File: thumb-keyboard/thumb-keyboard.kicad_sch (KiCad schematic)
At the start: 132 parts, among them J1 Conn_01x02_Socket, U1 nice_nano

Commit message: first commit after change to branch with optional B3F-1000 switches. footprint is going to be 144x60
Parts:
- added S100, S101, S102, S103, S104, S105, S106, S107, S108, S109, S110, S111, S112, S113, S114, S115, S116, S117, S118, S119, S120, S123, S61, S62, S64, S65, S66, S67, S68, S69, S70, S71, S72, S73, S74, S75, S76, S77, S78, S79, S80, S81, S82, S83, S84, S85, S86, S87, S88, S89, S90, S91, S92, S93, S94, S95, S96, S97, S98, S99: B3F-1000, B3F_1000:SW_B3F-1000, symbol B3F-1000:B3F-1000
- renumbered S62 to S121, S61 to S122
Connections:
- net C0R0D: now also S61.3, S61.4; no longer S63.1, S63.2
- net COL0: now also S109.1, S109.2, S61.1, S61.2, S73.1, S73.2, S85.1, S85.2, S97.1, S97.2; no longer S63.3, S63.4
- net COL1: now also S110.1, S110.2, S62.1, S62.2, S74.1, S74.2, S86.1, S86.2, S98.1, S98.2; no longer U1.12 (P1.06)
- net COL10: now also U1.20 (AIN7/P0.31), S107.1, S107.2, S119.1, S119.2, S71.1, S71.2, S83.1, S83.2, S95.1, S95.2
- net COL11: now also S108.1, S108.2, S120.1, S120.2, S72.1, S72.2, S84.1, S84.2, S96.1, S96.2
- net COL2: now also S63.1, S63.2, S111.1, S111.2, S75.1, S75.2, S87.1, S87.2, S99.1, S99.2
- net COL3: now also S100.1, S100.2, S112.1, S112.2, S64.1, S64.2, S76.1, S76.2, S88.1, S88.2
- net COL4: now also S101.1, S101.2, S113.1, S113.2, S65.1, S65.2, S77.1, S77.2, S89.1, S89.2
- net COL5: now also S102.1, S102.2, S114.1, S114.2, S66.1, S66.2, S78.1, S78.2, S90.1, S90.2
- net COL6: now also S103.1, S103.2, S115.1, S115.2, S67.1, S67.2, S79.1, S79.2, S91.1, S91.2
- net COL7: now also S104.1, S104.2, S116.1, S116.2, S68.1, S68.2, S80.1, S80.2, S92.1, S92.2
- net COL8: now also S105.1, S105.2, S117.1, S117.2, S69.1, S69.2, S81.1, S81.2, S93.1, S93.2
- net COL9: now also U1.12 (P1.06), S106.1, S106.2, S118.1, S118.2, S70.1, S70.2, S82.1, S82.2, S94.1, S94.2
- net GND: now also S123.3, S123.4
- net ROW2: no longer U1.20 (AIN7/P0.31)
- net RST: now also S123.1, S123.2
- net C7R2D: now reaches D32.2 (A), S32.3, S32.4
- net C7R2D: now also S92.3, S92.4
- net C5R2D: now reaches D30.2 (A), S30.3, S30.4
- net C5R2D: now also S90.3, S90.4
- net C2R2D: now reaches D27.2 (A), S27.3, S27.4
- net C2R2D: now also S87.3, S87.4
- net C1R0D: now reaches D2.2 (A), S2.3, S2.4
- net C1R0D: now also S62.3, S62.4
- net C4R4D: now reaches D53.2 (A), S53.3, S53.4
- net C4R4D: now also S113.3, S113.4
- net C11R2D: now reaches D36.2 (A), S36.3, S36.4
- net C11R2D: now also S96.3, S96.4
- net C4R0D: now reaches D5.2 (A), S5.3, S5.4
- net C4R0D: now also S65.3, S65.4
- net C3R4D: now reaches D52.2 (A), S52.3, S52.4
- net C3R4D: now also S112.3, S112.4
- net C6R2D: now reaches D31.2 (A), S31.3, S31.4
- net C6R2D: now also S91.3, S91.4
- net C9R2D: now reaches D34.2 (A), S34.3, S34.4
- net C9R2D: now also S94.3, S94.4
- net C8R2D: now reaches D33.2 (A), S33.3, S33.4
- net C8R2D: now also S93.3, S93.4
- net C1R4D: now reaches D50.2 (A), S50.3, S50.4
- net C1R4D: now also S110.3, S110.4
- net C10R2D: now reaches D35.2 (A), S35.3, S35.4
- net C10R2D: now also S95.3, S95.4
- net C6R1D: now reaches D19.2 (A), S19.3, S19.4
- net C6R1D: now also S79.3, S79.4
- net C9R1D: now reaches D22.2 (A), S22.3, S22.4
- net C9R1D: now also S82.3, S82.4
- net C2R1D: now reaches D15.2 (A), S15.3, S15.4
- net C2R1D: now also S75.3, S75.4
- net C0R3D: now reaches D37.2 (A), S37.3, S37.4
- net C0R3D: now also S97.3, S97.4
- net C9R0D: now reaches D10.2 (A), S10.3, S10.4
- net C9R0D: now also S70.3, S70.4
- net C5R4D: now reaches D54.2 (A), S54.3, S54.4
- net C5R4D: now also S114.3, S114.4
- net C0R1D: now reaches D13.2 (A), S13.3, S13.4
- net C0R1D: now also S73.3, S73.4
- net C11R1D: now reaches D24.2 (A), S24.3, S24.4
- net C11R1D: now also S84.3, S84.4
- net C9R4D: now reaches D58.2 (A), S58.3, S58.4
- net C9R4D: now also S118.3, S118.4
- net C4R1D: now reaches D17.2 (A), S17.3, S17.4
- net C4R1D: now also S77.3, S77.4
- net C11R0D: now reaches D12.2 (A), S12.3, S12.4
- net C11R0D: now also S72.3, S72.4
- net C2R3D: now reaches D39.2 (A), S39.3, S39.4
- net C2R3D: now also S99.3, S99.4
- net C10R4D: now reaches D59.2 (A), S59.3, S59.4
- net C10R4D: now also S119.3, S119.4
- net C1R3D: now reaches D38.2 (A), S38.3, S38.4
- net C1R3D: now also S98.3, S98.4
- net C0R4D: now reaches D49.2 (A), S49.3, S49.4
- net C0R4D: now also S109.3, S109.4
- net C0R2D: now reaches D25.2 (A), S25.3, S25.4
- net C0R2D: now also S85.3, S85.4
- net C5R0D: now reaches D6.2 (A), S6.3, S6.4
- net C5R0D: now also S66.3, S66.4
- net C5R1D: now reaches D18.2 (A), S18.3, S18.4
- net C5R1D: now also S78.3, S78.4
- net C6R0D: now reaches D7.2 (A), S7.3, S7.4
- net C6R0D: now also S67.3, S67.4
- net C11R3D: now reaches D48.2 (A), S48.3, S48.4
- net C11R3D: now also S108.3, S108.4
- net C4R3D: now reaches D41.2 (A), S41.3, S41.4
- net C4R3D: now also S101.3, S101.4
- net C10R0D: now reaches D11.2 (A), S11.3, S11.4
- net C10R0D: now also S71.3, S71.4
- net C11R4D: now reaches D60.2 (A), S60.3, S60.4
- net C11R4D: now also S120.3, S120.4
- net C10R3D: now reaches D47.2 (A), S47.3, S47.4
- net C10R3D: now also S107.3, S107.4
- net C2R4D: now reaches D51.2 (A), S51.3, S51.4
- net C2R4D: now also S111.3, S111.4
- net C1R2D: now reaches D26.2 (A), S26.3, S26.4
- net C1R2D: now also S86.3, S86.4
- net C7R1D: now reaches D20.2 (A), S20.3, S20.4
- net C7R1D: now also S80.3, S80.4
- net C3R1D: now reaches D16.2 (A), S16.3, S16.4
- net C3R1D: now also S76.3, S76.4
- net C6R4D: now reaches D55.2 (A), S55.3, S55.4
- net C6R4D: now also S115.3, S115.4
- net C3R3D: now reaches D40.2 (A), S40.3, S40.4
- net C3R3D: now also S100.3, S100.4
- net C8R0D: now reaches D9.2 (A), S9.3, S9.4
- net C8R0D: now also S69.3, S69.4
- net C10R1D: now reaches D23.2 (A), S23.3, S23.4
- net C10R1D: now also S83.3, S83.4
- net C4R2D: now reaches D29.2 (A), S29.3, S29.4
- net C4R2D: now also S89.3, S89.4
- net C2R0D: now reaches D3.2 (A), S3.3, S3.4
- net C2R0D: now also S63.3, S63.4
- net C7R0D: now reaches D8.2 (A), S8.3, S8.4
- net C7R0D: now also S68.3, S68.4
- net C8R4D: now reaches D57.2 (A), S57.3, S57.4
- net C8R4D: now also S117.3, S117.4
- net C8R1D: now reaches D21.2 (A), S21.3, S21.4
- net C8R1D: now also S81.3, S81.4
- net C7R3D: now reaches D44.2 (A), S44.3, S44.4
- net C7R3D: now also S104.3, S104.4
- net C6R3D: now reaches D43.2 (A), S43.3, S43.4
- net C6R3D: now also S103.3, S103.4
- net C9R3D: now reaches D46.2 (A), S46.3, S46.4
- net C9R3D: now also S106.3, S106.4
- net C5R3D: now reaches D42.2 (A), S42.3, S42.4
- net C5R3D: now also S102.3, S102.4
- net C3R2D: now reaches D28.2 (A), S28.3, S28.4
- net C3R2D: now also S88.3, S88.4
- net C7R4D: now reaches D56.2 (A), S56.3, S56.4
- net C7R4D: now also S116.3, S116.4
- net C8R3D: now reaches D45.2 (A), S45.3, S45.4
- net C8R3D: now also S105.3, S105.4
- net C1R1D: now reaches D14.2 (A), S14.3, S14.4
- net C1R1D: now also S74.3, S74.4
- net C3R0D: now reaches D4.2 (A), S4.3, S4.4
- net C3R0D: now also S64.3, S64.4
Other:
- moved on the sheet: D61, D62, D63, D64, D65, D66, D67, S121, S122

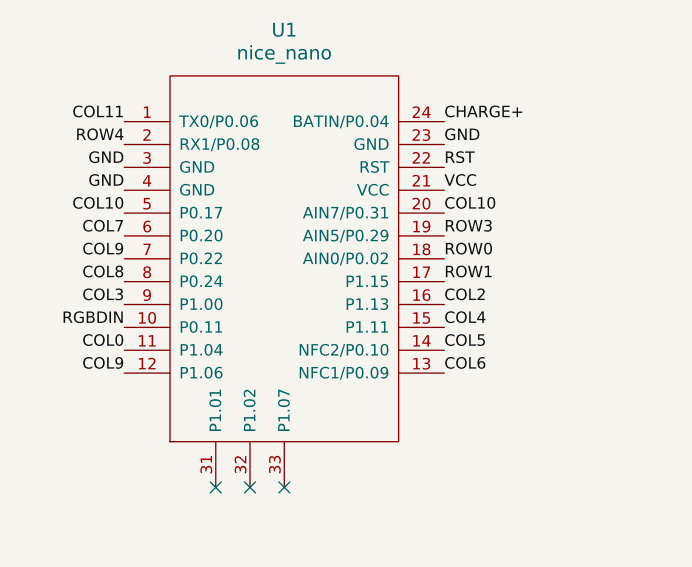
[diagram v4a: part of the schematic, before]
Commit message: have something that looks alright. max size of 144x60mm. A little concerning how messy it is though
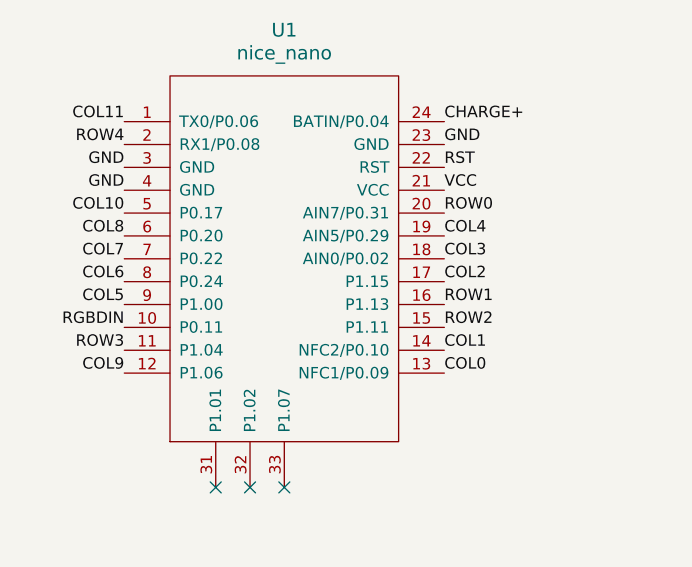
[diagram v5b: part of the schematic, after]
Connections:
- net COL0: now also U1.13 (NFC1/P0.09); no longer U1.11 (P1.04)
- net COL1: now also U1.14 (NFC2/P0.10)
- net COL10: no longer U1.20 (AIN7/P0.31)
- net COL2: now also U1.17 (P1.15); no longer U1.16 (P1.13)
- net COL3: now also U1.18 (AIN0/P0.02); no longer U1.9 (P1.00)
- net COL4: now also U1.19 (AIN5/P0.29); no longer U1.15 (P1.11)
- net COL5: now also U1.9 (P1.00); no longer U1.14 (NFC2/P0.10)
- net COL6: now also U1.8 (P0.24); no longer U1.13 (NFC1/P0.09)
- net COL7: now also U1.7 (P0.22); no longer U1.6 (P0.20)
- net COL8: now also U1.6 (P0.20); no longer U1.8 (P0.24)
- net COL9: no longer U1.7 (P0.22)
- net ROW0: now also U1.20 (AIN7/P0.31); no longer U1.18 (AIN0/P0.02)
- net ROW1: now also U1.16 (P1.13); no longer U1.17 (P1.15)
- net ROW2: now also U1.15 (P1.11)
- net ROW3: now also U1.11 (P1.04); no longer U1.19 (AIN5/P0.29)
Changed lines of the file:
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@@
 		)
 	)
+	(label "COL8"
+		(at 26.67 52.07 180)
+		(effects
+			(font
+				(size 1.27 1.27)
+			)
+			(justify right bottom)
+		)
+	)
 	(label "RST"
 		(at 116.84 488.95 0)
@@
 		)
 	)
-	(label "COL0"
-		(at 26.67 64.77 180)
-		(effects
-			(font
-				(size 1.27 1.27)
-			)
-			(justify right bottom)
-		)
-	)
 	(label "C8R4D"
 		(at 280.67 361.95 0)
@@
 		)
 	)
-	(label "ROW3"
-		(at 62.23 52.07 0)
-		(effects
-			(font
-				(size 1.27 1.27)
-			)
-			(justify left bottom)
-		)
-	)
 	(label "C7R4D"
 		(at 251.46 387.35 0)
@@
 		)
 	)
-	(label "COL5"
-		(at 62.23 64.77 0)
-		(effects
-			(font
-				(size 1.27 1.27)
-			)
-			(justify left bottom)
-		)
-	)
 	(label "COL11"
 		(at 358.14 300.99 180)
@@
 		)
 	)
-	(label "C1R0D"
-		(at 76.2 266.7 0)
+	(label "COL5"
+		(at 26.67 59.69 180)
+		(effects
+			(font
+				(size 1.27 1.27)
+			)
+			(justify right bottom)
+		)
+	)
+	(label "ROW2"
+		(at 62.23 62.23 0)
 		(effects
 			(font
@@
 		)
 	)
-	(label "C7R1D"
-		(at 461.01 71.12 90)
+	(label "C1R0D"
+		(at 76.2 266.7 0)
 		(effects
 			(font
@@
 		)
 	)
-	(label "ROW1"
-		(at 62.23 57.15 0)
+	(label "C7R1D"
+		(at 461.01 71.12 90)
 		(effects
 			(font
@@
 		)
 	)
-	(label "COL3"
-		(at 26.67 59.69 180)
-		(effects
-			(font
-				(size 1.27 1.27)
-			)
-			(justify right bottom)
-		)
-	)
 	(label "C4R0D"
 		(at 163.83 266.7 0)
@@
 		)
 	)
-	(label "COL6"
-		(at 62.23 67.31 0)
-		(effects
-			(font
-				(size 1.27 1.27)
-			)
-			(justify left bottom)
-		)
-	)
 	(label "C6R2D"
 		(at 416.56 96.52 90)
@@
 		)
 	)
-	(label "COL9"
-		(at 26.67 54.61 180)
-		(fields_autoplaced yes)
-		(effects
-			(font
-				(size 1.27 1.27)
-			)
-			(justify right bottom)
-		)
-		(property "Netclass" "Default"
-			(at 26.67 55.88 0)
-			(effects
-				(font
-					(size 1.27 1.27)
-					(italic yes)
-				)
-				(justify right)
-				(hide yes)
-			)
-		)
-	)
 	(label "C8R3D"
 		(at 280.67 331.47 0)
@@
 		)
 	)
+	(label "COL3"
+		(at 62.23 54.61 0)
+		(effects
+			(font
+				(size 1.27 1.27)
+			)
+			(justify left bottom)
+		)
+	)
 	(label "C2R0D"
 		(at 105.41 266.7 0)
@@
 		)
 	)
+	(label "COL7"
+		(at 26.67 54.61 180)
+		(effects
+			(font
+				(size 1.27 1.27)
+			)
+			(justify right bottom)
+		)
+	)
 	(label "COL8"
 		(at 270.51 241.3 180)
@@
 		)
 	)
-	(label "COL2"
-		(at 62.23 59.69 0)
+	(label "C9R3D"
+		(at 549.91 121.92 90)
 		(effects
 			(font
@@
 		)
 	)
-	(label "C9R3D"
-		(at 549.91 121.92 90)
+	(label "ROW3"
+		(at 26.67 64.77 180)
 		(effects
 			(font
 				(size 1.27 1.27)
 			)
-			(justify left bottom)
+			(justify right bottom)
 		)
 	)
@@
 		)
 	)
+	(label "ROW1"
+		(at 62.23 59.69 0)
+		(effects
+			(font
+				(size 1.27 1.27)
+			)
+			(justify left bottom)
+		)
+	)
 	(label "C5R2D"
 		(at 372.11 96.52 90)
@@
 		)
 	)
-	(label "ROW4"
-		(at 26.67 41.91 180)
-		(fields_autoplaced yes)
-		(effects
-			(font
-				(size 1.27 1.27)
-			)
-			(justify right bottom)
-		)
-		(property "Netclass" "Default"
-			(at 26.67 43.18 0)
-			(effects
-				(font
-					(size 1.27 1.27)
-					(italic yes)
-				)
-				(justify right)
-				(hide yes)
-			)
-		)
-	)
 	(label "GND"
 		(at 199.39 185.42 0)
@@
 		)
 	)
-	(label "ROW0"
-		(at 62.23 54.61 0)
-		(effects
-			(font
-				(size 1.27 1.27)
-			)
-			(justify left bottom)
-		)
-	)
 	(label "C0R1D"
 		(at 46.99 295.91 0)
@@
 		)
 	)
-	(label "COL10"
-		(at 62.23 49.53 0)
-		(effects
-			(font
-				(size 1.27 1.27)
-			)
-			(justify left bottom)
-		)
-	)
 	(label "COL11"
 		(at 358.14 361.95 180)
@@
 		)
 	)
+	(label "ROW4"
+		(at 26.67 41.91 180)
+		(fields_autoplaced yes)
+		(effects
+			(font
+				(size 1.27 1.27)
+			)
+			(justify right bottom)
+		)
+		(property "Netclass" "Default"
+			(at 26.67 43.18 0)
+			(effects
+				(font
+					(size 1.27 1.27)
+					(italic yes)
+				)
+				(justify right)
+				(hide yes)
+			)
+		)
+	)
 	(label "C1R4D"
 		(at 76.2 361.95 0)
@@
 		)
 	)
-	(label "COL7"
-		(at 26.67 52.07 180)
-		(effects
-			(font
-				(size 1.27 1.27)
-			)
-			(justify right bottom)
-		)
-	)
 	(label "COL5"
 		(at 182.88 266.7 180)
@@
 		)
 	)
+	(label "COL6"
+		(at 26.67 57.15 180)
+		(effects
+			(font
+				(size 1.27 1.27)
+			)
+			(justify right bottom)
+		)
+	)
 	(label "COL4"
 		(at 153.67 270.51 180)
@@
 		)
 	)
+	(label "COL4"
+		(at 62.23 52.07 0)
+		(effects
+			(font
+				(size 1.27 1.27)
+			)
+			(justify left bottom)
+		)
+	)
 	(label "C1R0D"
 		(at 194.31 45.72 90)
@@
 	)
 	(label "COL8"
-		(at 26.67 57.15 180)
-		(effects
-			(font
-				(size 1.27 1.27)
-			)
-			(justify right bottom)
-		)
-	)
-	(label "COL8"
 		(at 270.51 387.35 180)
 		(effects
@@
 		)
 	)
+	(label "COL0"
+		(at 62.23 67.31 0)
+		(effects
+			(font
+				(size 1.27 1.27)
+			)
+			(justify left bottom)
+		)
+	)
 	(label "C9R1D"
 		(at 309.88 295.91 0)
@@
 		)
 	)
+	(label "COL2"
+		(at 62.23 57.15 0)
+		(effects
+			(font
+				(size 1.27 1.27)
+			)
+			(justify left bottom)
+		)
+	)
+	(label "COL10"
+		(at 26.67 49.53 180)
+		(effects
+			(font
+				(size 1.27 1.27)
+			)
+			(justify right bottom)
+		)
+	)
 	(label "VCC"
 		(at 290.83 175.26 0)
@@
 		)
 	)
-	(label "COL4"
-		(at 62.23 62.23 0)
-		(effects
-			(font
-				(size 1.27 1.27)
-			)
-			(justify left bottom)
-		)
-	)
 	(label "C8R3D"
 		(at 280.67 356.87 0)
@@
 		)
 	)
-	(label "COL10"
-		(at 26.67 49.53 180)
-		(effects
-			(font
-				(size 1.27 1.27)
-			)
-			(justify right bottom)
-		)
-	)
 	(label "C6R3D"
 		(at 222.25 356.87 0)
@@
 		)
 	)
+	(label "ROW0"
+		(at 62.23 49.53 0)
+		(effects
+			(font
+				(size 1.27 1.27)
+			)
+			(justify left bottom)
+		)
+	)
 	(label "C3R4D"
 		(at 134.62 387.35 0)
@@
 		(effects
 			(font
+				(size 1.27 1.27)
+			)
+			(justify left bottom)
+		)
+	)
+	(label "COL1"
+		(at 62.23 64.77 0)
+		(effects
+			(font

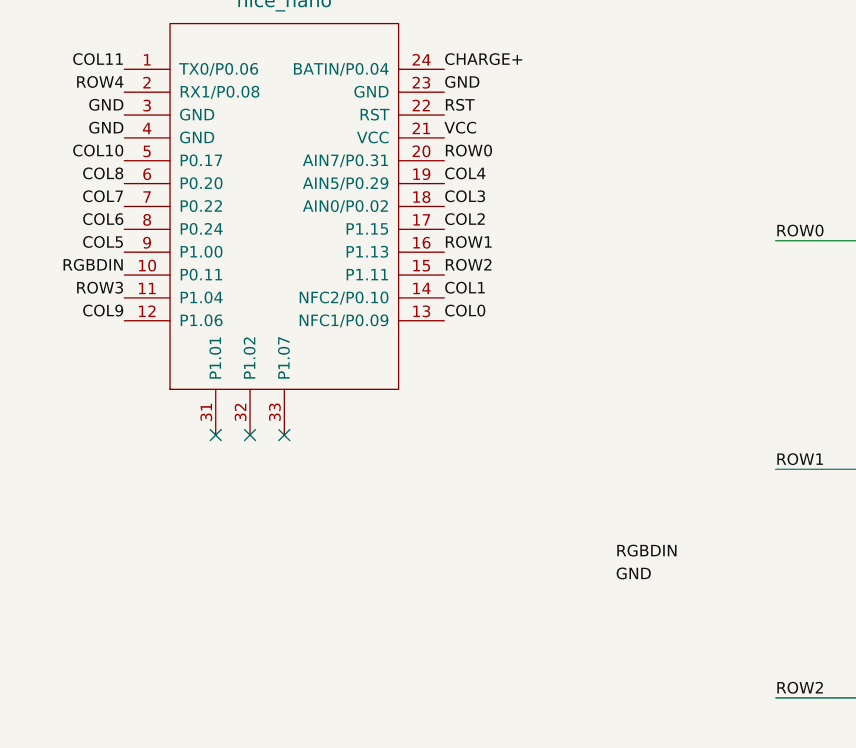
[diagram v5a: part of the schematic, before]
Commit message: sent out v1.0 pcb order
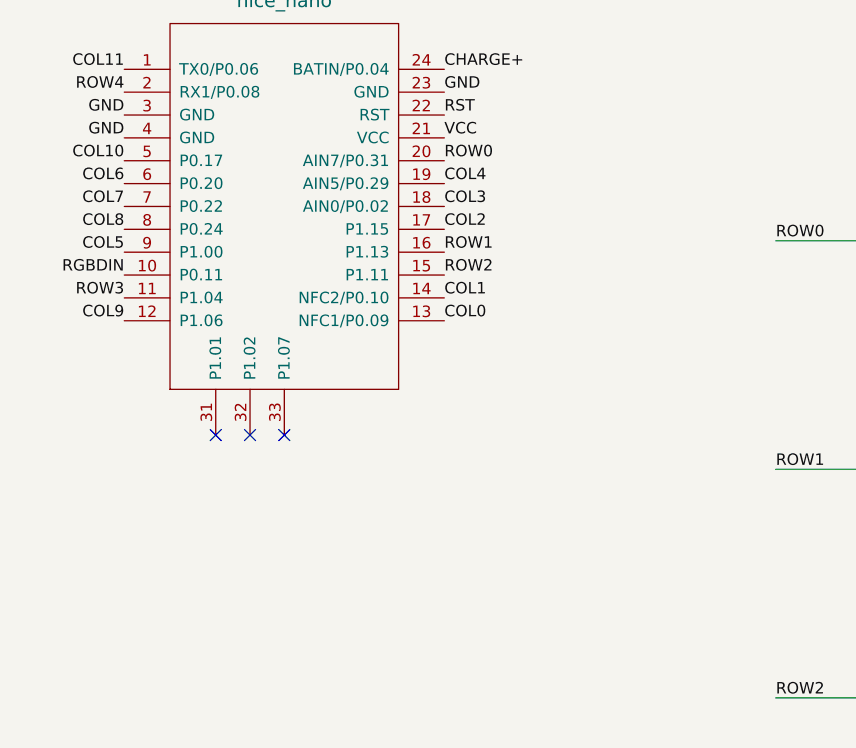
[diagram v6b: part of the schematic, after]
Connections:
- net COL6: now also U1.6 (P0.20); no longer U1.8 (P0.24)
- net COL8: now also U1.8 (P0.24); no longer U1.6 (P0.20)
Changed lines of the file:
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@@
 	)
 	(label "COL8"
-		(at 26.67 52.07 180)
+		(at 26.67 57.15 180)
 		(effects
 			(font
@@
 		)
 	)
-	(label "RGBDIN"
-		(at 81.28 93.98 0)
-		(effects
-			(font
-				(size 1.27 1.27)
-			)
-			(justify left bottom)
-		)
-	)
 	(label "C8R2D"
 		(at 280.67 326.39 0)
@@
 		)
 	)
-	(label "GND"
-		(at 81.28 96.52 0)
-		(fields_autoplaced yes)
-		(effects
-			(font
-				(size 1.27 1.27)
-			)
-			(justify left bottom)
-		)
-		(property "Netclass" "power"
-			(at 81.28 97.79 0)
-			(effects
-				(font
-					(size 1.27 1.27)
-					(italic yes)
-				)
-				(justify left)
-				(hide yes)
-			)
-		)
-	)
 	(label "C9R2D"
 		(at 549.91 96.52 90)
@@
 		)
 	)
+	(label "COL0"
+		(at 62.23 67.31 0)
+		(effects
+			(font
+				(size 1.27 1.27)
+			)
+			(justify left bottom)
+		)
+	)
 	(label "COL11"
 		(at 26.67 39.37 180)
@@
 		)
 	)
+	(label "COL1"
+		(at 62.23 64.77 0)
+		(effects
+			(font
+				(size 1.27 1.27)
+			)
+			(justify left bottom)
+		)
+	)
 	(label "C11R3D"
 		(at 368.3 356.87 0)
@@
 		)
 	)
-	(label "COL6"
-		(at 26.67 57.15 180)
-		(effects
-			(font
-				(size 1.27 1.27)
-			)
-			(justify right bottom)
-		)
-	)
 	(label "COL4"
 		(at 153.67 270.51 180)
@@
 		)
 	)
-	(label "COL0"
-		(at 62.23 67.31 0)
-		(effects
-			(font
-				(size 1.27 1.27)
-			)
-			(justify left bottom)
-		)
-	)
 	(label "C9R1D"
 		(at 309.88 295.91 0)
@@
 		)
 	)
+	(label "COL6"
+		(at 26.67 52.07 180)
+		(effects
+			(font
+				(size 1.27 1.27)
+			)
+			(justify right bottom)
+		)
+	)
 	(label "C10R2D"
 		(at 339.09 300.99 0)
@@
 		(effects
 			(font
-				(size 1.27 1.27)
-			)
-			(justify left bottom)
-		)
-	)
-	(label "COL1"
-		(at 62.23 64.77 0)
-		(effects
-			(font
